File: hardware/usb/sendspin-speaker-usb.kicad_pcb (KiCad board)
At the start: 2 copper layers, 0 parts

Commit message: hardware: footprints and nets in all three boards, JLC design rules
- Update PCB from Schematic on main, front panel and USB-C board.
- Design rules for JLCPCB 2-layer (0.15 mm track/clearance, 0.3 mm
  drill, 0.6 mm vias, 0.3 mm to the edge); net classes Power (1.0 mm),
  Speaker (0.6 mm), Supply3V3 (0.4 mm).
- TP4056 on the SOIC-8-EP footprint without 0.2 mm thermal vias;
  MSK12C02 footprint marked SMD, its shell pads to GND.
- Generator keeps symbol UUIDs stable so regenerated sheets stay linked.

Co-Authored-By: Claude Opus 5.5 <noreply@anthropic.com>
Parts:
- added J701: J_USB, Connector_JST:JST_XH_B4B-XH-A_1x04_P2.50mm_Vertical, F.Cu at (145.5, 102.4)
- added R701: 5.1k, Resistor_SMD:R_0805_2012Metric, F.Cu at (155.9, 108.3)
- added R702: 5.1k, Resistor_SMD:R_0805_2012Metric, F.Cu at (155.9, 111.2)
- added U701: USBLC6-2SC6, Package_TO_SOT_SMD:SOT-23-6, F.Cu at (156.3, 115.1)
- added USB701: USB-C, Connector_USB:USB_C_Receptacle_HRO_TYPE-C-31-M-12, F.Cu at (147.8, 112.6)

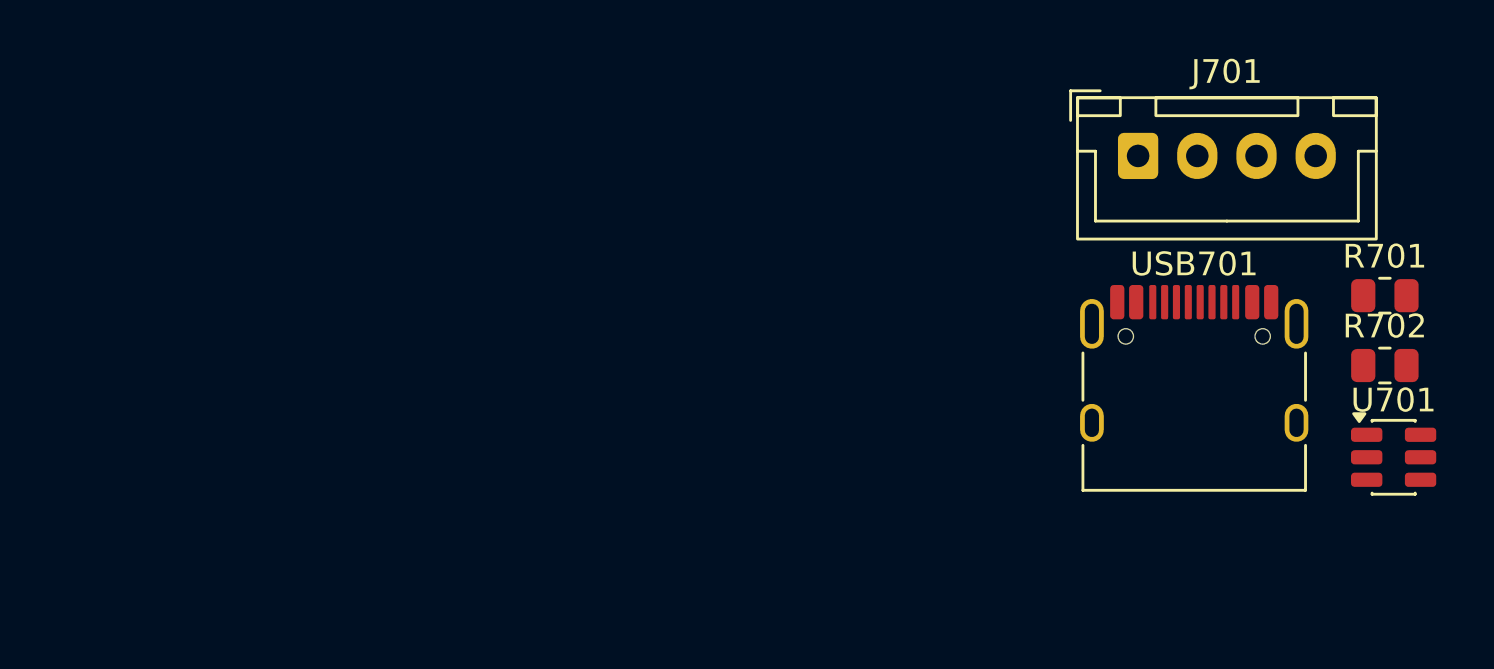
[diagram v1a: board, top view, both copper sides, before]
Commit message: hardware: first placement of all three boards
Outlines, mounting holes, edge connectors, parts by function and GND
pours, written with KiCad's Python (scripts/pcbplace.py, place_*.py).
DRC: no copper or courtyard errors; unrouted connections and silkscreen
text remain. Renders in hardware/docs/.

Co-Authored-By: Claude Opus 5.5 <noreply@anthropic.com>
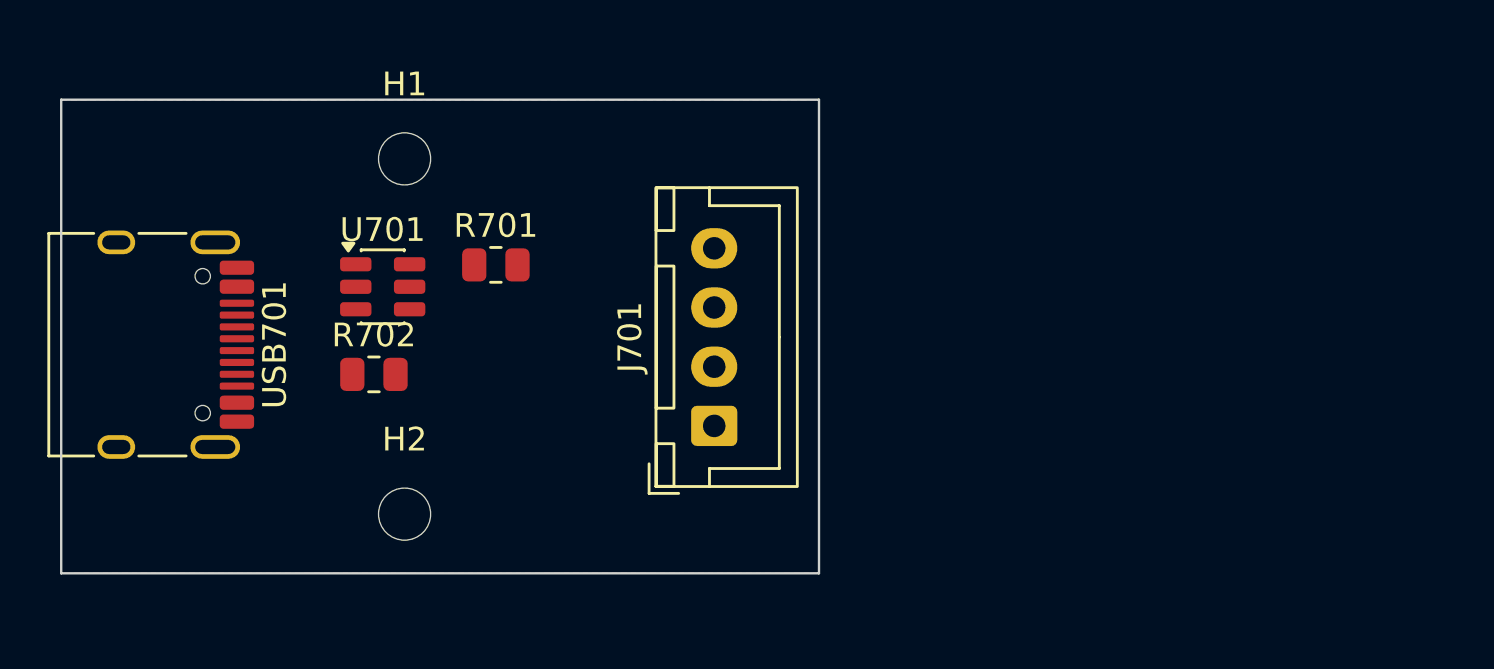
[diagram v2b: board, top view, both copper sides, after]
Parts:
- added H1: MountingHole_2.2mm_M2, MountingHole:MountingHole_2.2mm_M2, F.Cu at (114.5, 102.5)
- added H2: MountingHole_2.2mm_M2, MountingHole:MountingHole_2.2mm_M2, F.Cu at (114.5, 117.5)
- moved USB701 44.5 mm to (103.4, 110.3), turned to -90 degrees
- moved U701 43.3 mm to (113.6, 107.9)
- moved R702 42.7 mm to (113.2, 111.6)
- moved R701 37.6 mm to (118.4, 107.0)
- moved J701 21.2 mm to (127.6, 113.8), turned to 90 degrees
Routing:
- added copper zone on B.Cu, net GND
- added copper zone on F.Cu, net GND
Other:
- board outline added: 32 x 20 mm

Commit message: hardware: bare panel/USB-C boards updated, XH battery, holes in, round corners
- Boards updated from the schematics: J_USB XH 6 with CC1/CC2, panel
  without parts (J604 LED header), USB-C board without parts.
- J_BAT JST XH 2.
- M3 holes 4.5 mm in from the edges (heads stay on the board), M2 3 mm;
  rounded corners. DRC: no copper, courtyard or outline errors.

Co-Authored-By: Claude Opus 5.5 <noreply@anthropic.com>
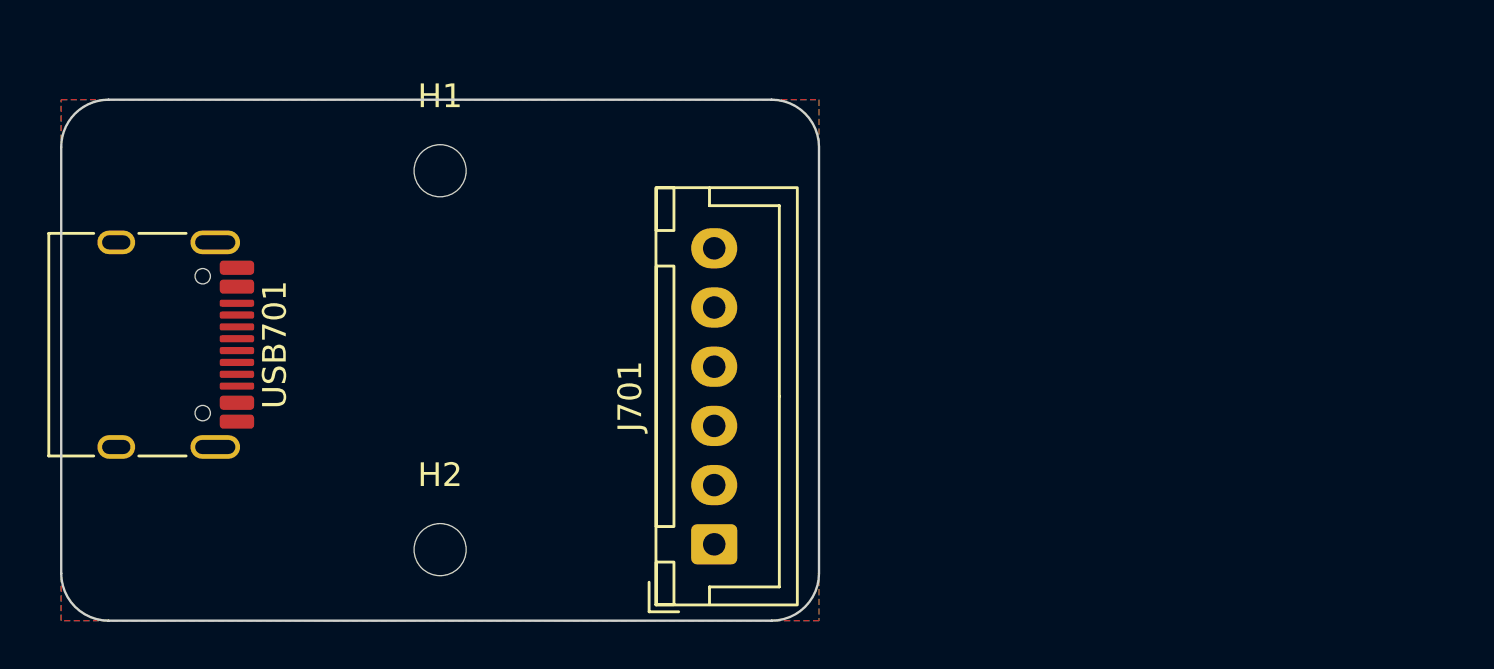
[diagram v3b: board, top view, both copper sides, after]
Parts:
- removed R701, R702: 5.1k, Resistor_SMD:R_0805_2012Metric
- removed U701: USBLC6-2SC6, Package_TO_SOT_SMD:SOT-23-6
- J701: footprint Connector_JST:JST_XH_B4B-XH-A_1x04_P2.50mm_Vertical -> Connector_JST:JST_XH_B6B-XH-A_1x06_P2.50mm_Vertical
- moved J701 5.00 mm to (127.6, 118.8)
- moved H2 2.12 mm to (116.0, 119.0)
- moved H1 1.58 mm to (116.0, 103.0)
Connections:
- J701 pad 4: GND -> /CC1
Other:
- board size 32 x 20 mm -> 32 x 22 mm
